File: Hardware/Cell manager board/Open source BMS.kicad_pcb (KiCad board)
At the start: 2 copper layers, 49 x 49 mm, 53 parts, among them P1 CONN_01X07, P2 EXT-TMP, P3 CONN_01X09, P4 CONN_01X09, Q1 BSS138, Q2 BSS138, Q3 BSS138, Q4 BSS138, Q5 BSS138, Q6 BSS138, U1 ATA6870N_BMS

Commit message: Changed 10uf cap and added slave BOM
Changed the 10uf cap to one that is slightly smaller and 1/5th the
price. (at the expense of voltage, 100v>35v) Also added a BOM for the
Cell manager slave board with all parts but the thermistor and
assosiated resistors
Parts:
- 10uF1: footprint Capacitors_SMD:C_2220 -> Capacitors_SMD:C_1206
- P1: footprint Pin_Header_Angled_1x07 -> Pin_Headers:Pin_Header_Angled_1x07
- Q1, Q2, Q3, Q4, Q5, Q6: footprint SOT-23 -> SMD_Packages:SOT-23
- moved 10uF1 3.08 mm to (203.2, 119.1), turned to 270 degrees
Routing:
- net GND: track 143.1 -> 163.6 mm, vias 16 -> 17
- net +BATT: track 18.8 -> 19.5 mm

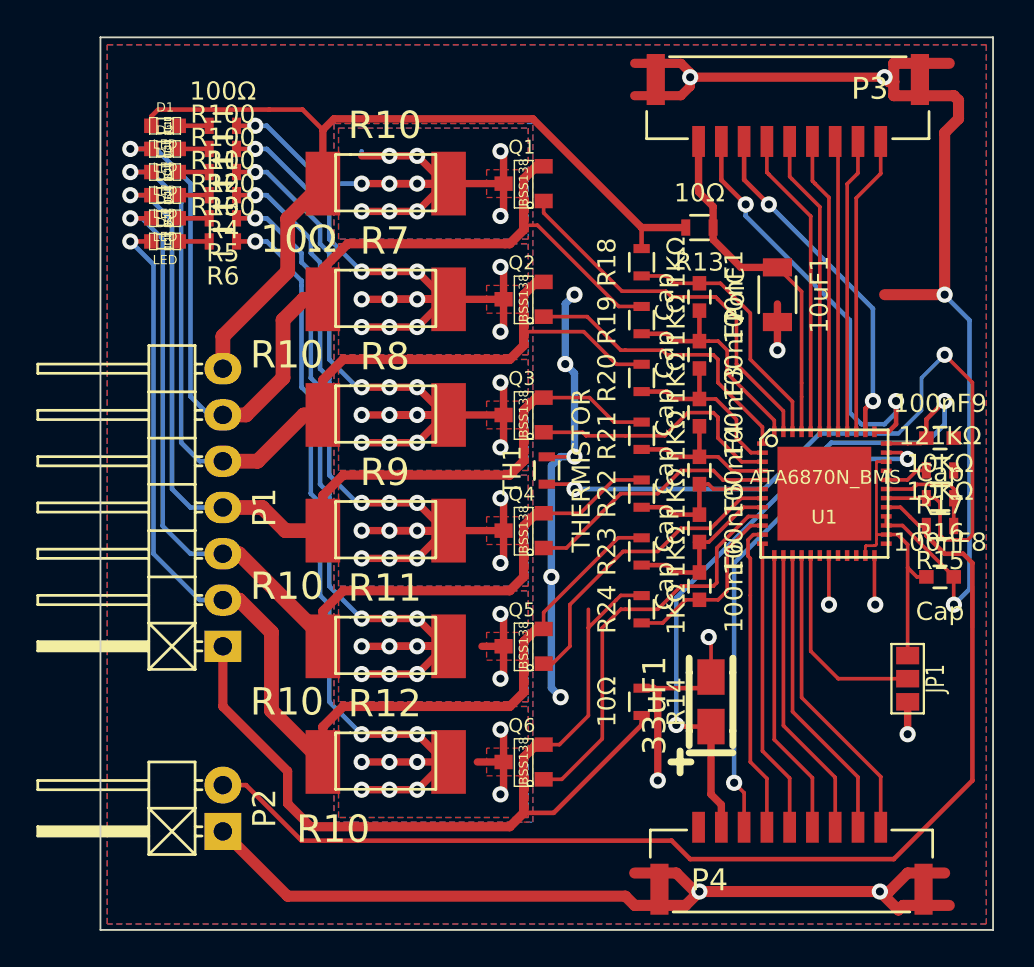
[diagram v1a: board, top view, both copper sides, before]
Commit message: cleaned up silkscreen and improved readme
Improved the readme file and added MicroMaster board to it. Also cleaned
up the Slave balance board's silkscreen
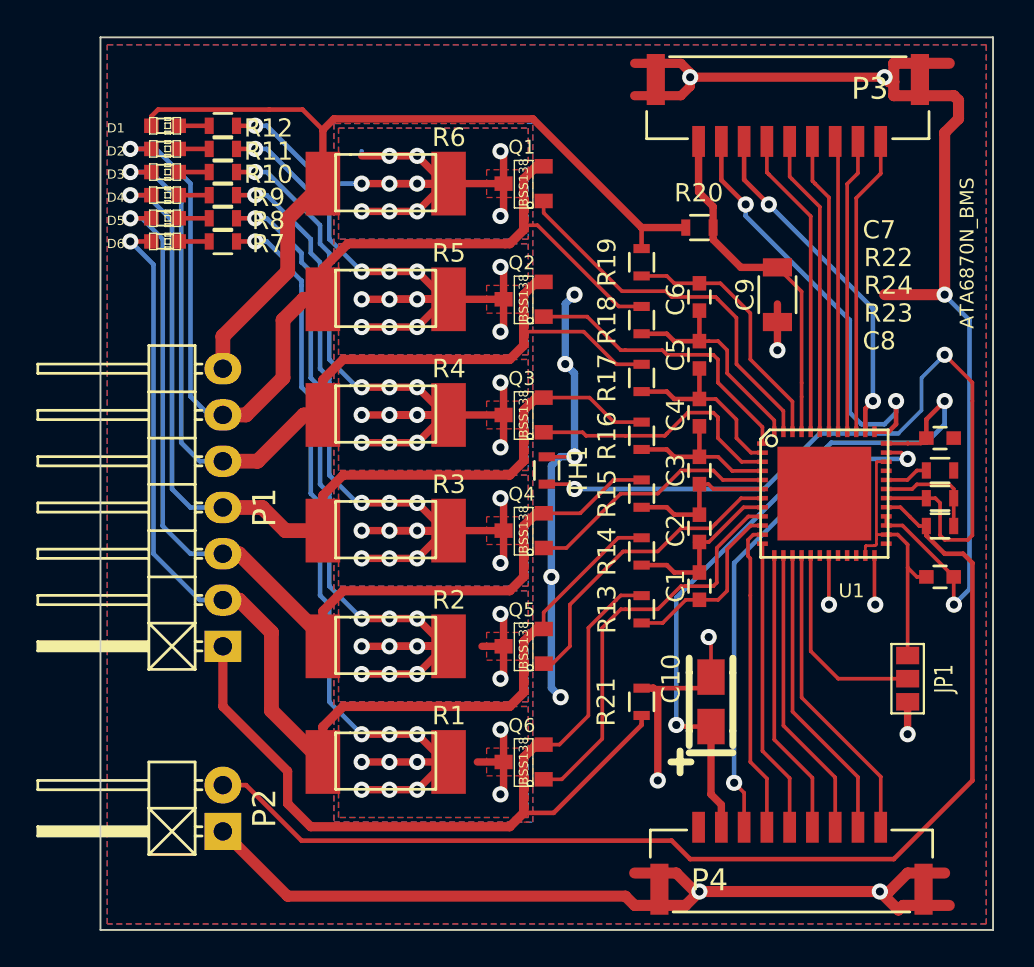
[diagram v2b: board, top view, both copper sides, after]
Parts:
- removed 10uF1: PolC, Capacitors_SMD:C_1206
- added C9: 10uF PolC, Capacitors_SMD:C_1206, F.Cu at (203.2, 119.1)
- C1: renamed from 100nF6; value Cap -> 100nF
- C10: renamed from 33uF1; value PolC -> 33uF PolC
- C2: renamed from 100nF5; value Cap -> 100nF
- C3: renamed from 100nF4; value Cap -> 100nF
- C4: renamed from 100nF3; value Cap -> 100nF
- C5: renamed from 100nF2; value Cap -> 100nF
- C6: renamed from 100nF1; value Cap -> 100nF
- C7: renamed from 100nF9; value Cap -> 100nF
- C8: renamed from 100nF8; value Cap -> 100nF
- Q1, Q2, Q3, Q4, Q5, Q6: footprint SMD_Packages:SOT-23 -> SOT-23
- R1: renamed from R12; value R10 -> 10Ω
- R10: renamed from R3; value R100 -> 100Ω
- R11: renamed from R2; value R100 -> 100Ω
- R2: renamed from R11; value R10 -> 10Ω
- R3: renamed from R9; value R10 -> 10Ω
- R4: renamed from R8; value R10 -> 10Ω
- R5: renamed from R7; value R10 -> 10Ω
- R7: renamed from R6; value R100 -> 100Ω
- R8: renamed from R5; value R100 -> 100Ω
- R9: renamed from R4; value R100 -> 100Ω
- renumbered R1 to R12, R24 to R13, R23 to R14, R22 to R15, R21 to R16, R20 to R17, R19 to R18, R18 to R19, R13 to R20, R14 to R21, R17 to R22, R15 to R23, R16 to R24, R10 to R6
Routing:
- net (no net): track 2.54 -> 0.25 mm
- net Net-(P1-Pad1): track 50.0 -> 48.9 mm
